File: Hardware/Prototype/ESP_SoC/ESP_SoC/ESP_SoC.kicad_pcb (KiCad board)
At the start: 4 copper layers, 34.5 x 14.7 mm, 36 parts, among them J1 USB_A, J2 Conn_01x01, J3 Conn_01x01, P1 USB_C_Plug, SW1 RESET, SW2 BOOT, U1 AP2112K-3.3, U2 ESP32-S3FN8, Y1 40MHz

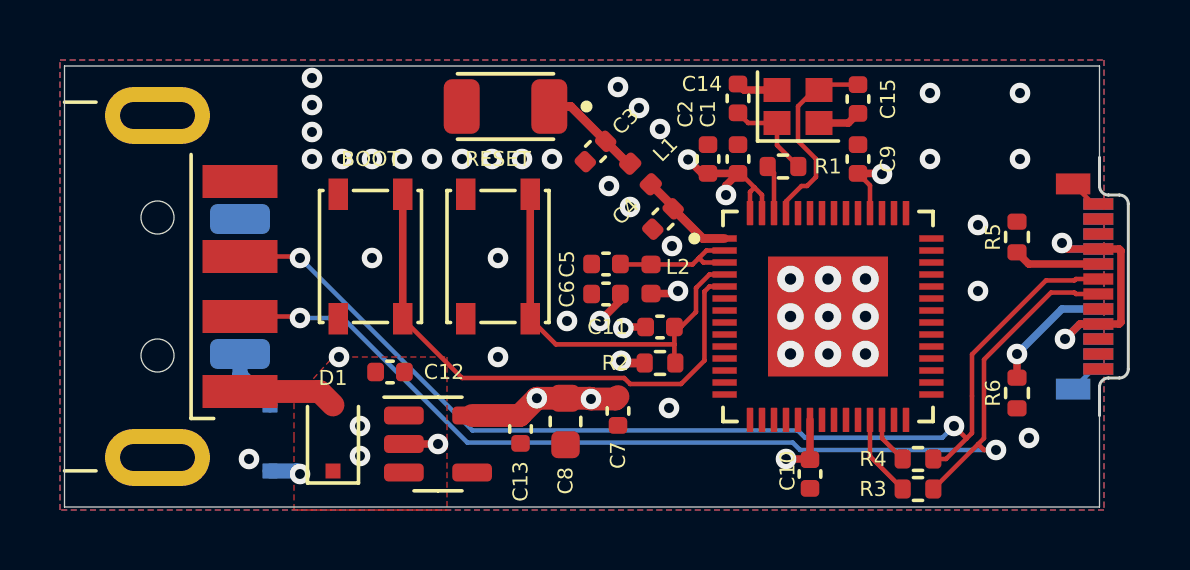
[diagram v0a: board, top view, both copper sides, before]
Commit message: Finished PCB prototypes and BOM
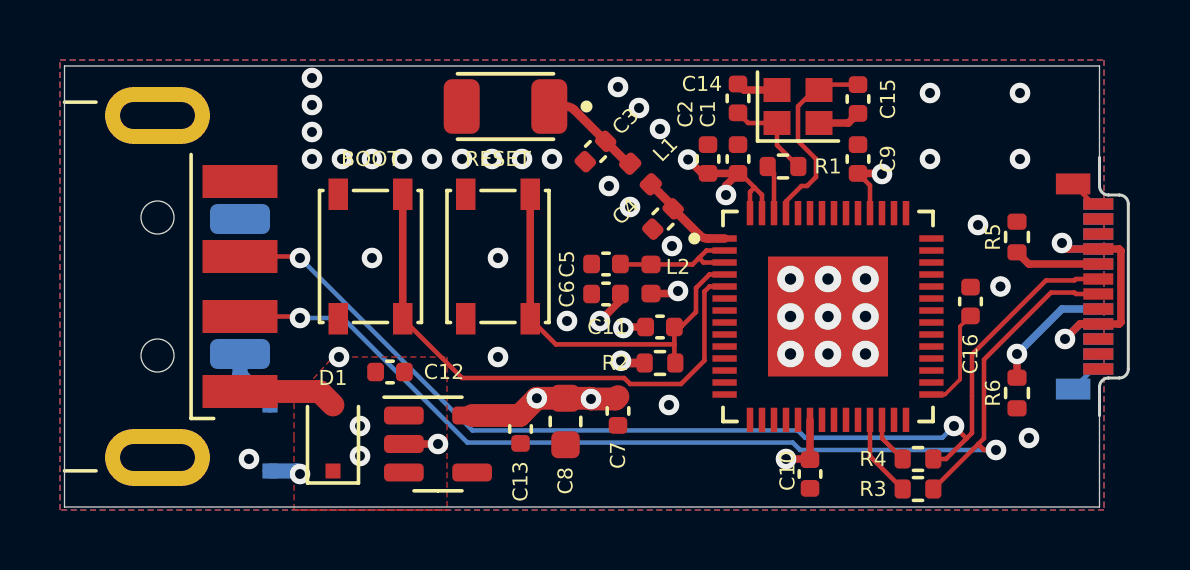
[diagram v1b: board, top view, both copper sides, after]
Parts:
- added C16: 1u, Capacitor_SMD:C_0402_1005Metric, F.Cu at (128.8, 99.2)
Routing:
- net VDD: track 0.00 -> 3.43 mm
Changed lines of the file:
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@@
     )
-  )
-  (footprint "clipboard:52b86674-39ac-4791-87c9-d1ce4ecf49a0" (layer "F.Cu")
-    (at 133.05 102.575 -90)
-    (fp_text reference "" (at 0 0 90) (layer "F.SilkS")
-      (effects (font (size 1.27 1.27) (thickness 0.15)))
-    )
-    (fp_text value "" (at 0 0 90) (layer "F.SilkS")
-      (effects (font (size 1.27 1.27) (thickness 0.15)))
-    )
-    (fp_line (start -6.875 -0.66) (end -6.875 -0.3) (layer "Edge.Cuts") (width 0.1))
-    (fp_line (start -6.575 -0.96) (end -1.075 -0.96) (layer "Edge.Cuts") (width 0.1))
-    (fp_line (start -0.475 0) (end 0.475 0) (layer "Edge.Cuts") (width 0.1))
-    (fp_line (start -0.775 -0.66) (end -0.775 -0.3) (layer "Edge.Cuts") (width 0.1))
-    (fp_line (start -7.175 0) (end -8.125 0) (layer "Edge.Cuts") (width 0.1))
-    (fp_arc (start -0.475 0) (mid -0.687132 -0.087868) (end -0.775 -0.3) (layer "Edge.Cuts") (width 0.1))
-    (fp_arc (start -6.875 -0.66) (mid -6.787132 -0.872132) (end -6.575 -0.96) (layer "Edge.Cuts") (width 0.1))
-    (fp_arc (start -6.875 -0.3) (mid -6.962868 -0.087868) (end -7.175 0) (layer "Edge.Cuts") (width 0.1))
-    (fp_arc (start -1.075 -0.96) (mid -0.862868 -0.872132) (end -0.775 -0.66) (layer "Edge.Cuts") (width 0.1))
   )
   (footprint "Inductor_SMD:L_0402_1005Metric" (layer "F.Cu")
@@
     )
   )
+  (footprint "clipboard:52b86674-39ac-4791-87c9-d1ce4ecf49a0" (layer "F.Cu")
+    (at 133.05 102.575 -90)
+    (fp_text reference "" (at 0 0 90) (layer "F.SilkS")
+      (effects (font (size 1.27 1.27) (thickness 0.15)))
+    )
+    (fp_text value "" (at 0 0 90) (layer "F.SilkS")
+      (effects (font (size 1.27 1.27) (thickness 0.15)))
+    )
+    (fp_line (start -6.875 -0.66) (end -6.875 -0.3) (layer "Edge.Cuts") (width 0.1))
+    (fp_line (start -6.575 -0.96) (end -1.075 -0.96) (layer "Edge.Cuts") (width 0.1))
+    (fp_line (start -0.475 0) (end 0.475 0) (layer "Edge.Cuts") (width 0.1))
+    (fp_line (start -0.775 -0.66) (end -0.775 -0.3) (layer "Edge.Cuts") (width 0.1))
+    (fp_line (start -7.175 0) (end -8.125 0) (layer "Edge.Cuts") (width 0.1))
+    (fp_arc (start -0.475 0) (mid -0.687132 -0.087868) (end -0.775 -0.3) (layer "Edge.Cuts") (width 0.1))
+    (fp_arc (start -6.875 -0.66) (mid -6.787132 -0.872132) (end -6.575 -0.96) (layer "Edge.Cuts") (width 0.1))
+    (fp_arc (start -6.875 -0.3) (mid -6.962868 -0.087868) (end -7.175 0) (layer "Edge.Cuts") (width 0.1))
+    (fp_arc (start -1.075 -0.96) (mid -0.862868 -0.872132) (end -0.775 -0.66) (layer "Edge.Cuts") (width 0.1))
+  )
   (footprint "Capacitor_SMD:C_0603_1608Metric" (layer "F.Cu")
     (at 115.25 103.25 -90)
@@
       (net 1 "+3V3") (pintype "passive"))
     (pad "2" smd roundrect (at 0.48 0 180) (size 0.56 0.62) (layers "F.Cu" "F.Paste" "F.Mask") (roundrect_rratio 0.25)
+      (net 2 "GND") (pintype "passive"))
+    (model "${KICAD6_3DMODEL_DIR}/Capacitor_SMD.3dshapes/C_0402_1005Metric.wrl"
+      (offset (xyz 0 0 0))
+      (scale (xyz 1 1 1))
+      (rotate (xyz 0 0 0))
+    )
+  )
+  (footprint "Capacitor_SMD:C_0402_1005Metric" (layer "F.Cu")
+    (at 128.75 99.25 90)
+    (descr "Capacitor SMD 0402 (1005 Metric), square (rectangular) end terminal, IPC_7351 nominal, (Body size source: IPC-SM-782 page 76, https://www.pcb-3d.com/wordpress/wp-content/uploads/ipc-sm-782a_amendment_1_and_2.pdf), generated with kicad-footprint-generator")
+    (tags "capacitor")
+    (property "Sheetfile" "ESP_SoC.kicad_sch")
+    (property "Sheetname" "")
+    (attr smd)
+    (fp_text reference "C16" (at -1.75 0 90) (layer "F.SilkS")
+      (effects (font (size 0.5 0.5) (thickness 0.125)))
+    )
+    (fp_text value "1u" (at 0 1.16 90) (layer "F.Fab")
+      (effects (font (size 1 1) (thickness 0.15)))
+    )
+    (fp_text user "${REFERENCE}" (at 0 0 90) (layer "F.Fab")
+      (effects (font (size 0.25 0.25) (thickness 0.04)))
+    )
+    (fp_line (start -0.107836 0.36) (end 0.107836 0.36) (layer "F.SilkS") (width 0.12))
+    (fp_line (start -0.107836 -0.36) (end 0.107836 -0.36) (layer "F.SilkS") (width 0.12))
+    (fp_line (start 0.91 0.46) (end -0.91 0.46) (layer "F.CrtYd") (width 0.05))
+    (fp_line (start -0.91 0.46) (end -0.91 -0.46) (layer "F.CrtYd") (width 0.05))
+    (fp_line (start 0.91 -0.46) (end 0.91 0.46) (layer "F.CrtYd") (width 0.05))
+    (fp_line (start -0.91 -0.46) (end 0.91 -0.46) (layer "F.CrtYd") (width 0.05))
+    (fp_line (start 0.5 -0.25) (end 0.5 0.25) (layer "F.Fab") (width 0.1))
+    (fp_line (start -0.5 -0.25) (end 0.5 -0.25) (layer "F.Fab") (width 0.1))
+    (fp_line (start -0.5 0.25) (end -0.5 -0.25) (layer "F.Fab") (width 0.1))
+    (fp_line (start 0.5 0.25) (end -0.5 0.25) (layer "F.Fab") (width 0.1))
+    (pad "1" smd roundrect (at -0.48 0 90) (size 0.56 0.62) (layers "F.Cu" "F.Paste" "F.Mask") (roundrect_rratio 0.25)
+      (net 57 "VDD") (pintype "passive"))
+    (pad "2" smd roundrect (at 0.48 0 90) (size 0.56 0.62) (layers "F.Cu" "F.Paste" "F.Mask") (roundrect_rratio 0.25)
       (net 2 "GND") (pintype "passive"))
     (model "${KICAD6_3DMODEL_DIR}/Capacitor_SMD.3dshapes/C_0402_1005Metric.wrl"
@@
   (via (at 109.8 94.5) (size 0.6858) (drill 0.3302) (layers "F.Cu" "B.Cu") (net 2))
   (via (at 114.8 94.5) (size 0.6858) (drill 0.3302) (layers "F.Cu" "B.Cu") (net 2))
-  (via (at 118.7 102.8) (size 0.6858) (drill 0.3302) (layers "F.Cu" "B.Cu") (net 2))
+  (via (at 118.7 102.7) (size 0.6858) (drill 0.3302) (layers "F.Cu" "B.Cu") (net 2))
   (via (at 124 101) (size 0.889) (drill 0.381) (layers "F.Cu" "B.Cu") (net 2))
   (via (at 118.8 97.4) (size 0.6858) (drill 0.3302) (layers "F.Cu" "B.Cu") (net 2))
@@
   (via (at 125.25 101) (size 0.889) (drill 0.381) (layers "F.Cu" "B.Cu") (net 2))
   (via (at 111.8 94.5) (size 0.6858) (drill 0.3302) (layers "F.Cu" "B.Cu") (net 2))
-  (via (at 129 98.9) (size 0.6858) (drill 0.3302) (layers "F.Cu" "B.Cu") (net 2))
+  (via (at 129.75 98.75) (size 0.6858) (drill 0.3302) (layers "F.Cu" "B.Cu") (net 2))
   (via (at 118.4 93.5) (size 0.6858) (drill 0.3302) (layers "F.Cu" "B.Cu") (net 2))
   (via (at 125.25 99.75) (size 0.889) (drill 0.381) (layers "F.Cu" "B.Cu") (net 2))
@@
   (segment (start 133.01 101.5) (end 132.84 101.5) (width 0.1542) (layer "B.Cu") (net 2))
   (segment (start 132.84 101.5) (end 132.17 102.17) (width 0.1542) (layer "B.Cu") (net 2))
-  (segment (start 119.828822 97.15) (end 118.839411 96.160589) (width 0.29337) (layer "F.Cu") (net 3))
+  (segment (start 119.711664 97.032842) (end 118.839411 96.160589) (width 0.29337) (layer "F.Cu") (net 3))
   (segment (start 118.839411 96.089411) (end 118.092947 95.342947) (width 0.29337) (layer "F.Cu") (net 3))
-  (segment (start 120.555 97.15) (end 119.828822 97.15) (width 0.29337) (layer "F.Cu") (net 3))
+  (segment (start 120.555 97.15) (end 119.994507 97.15) (width 0.29337) (layer "F.Cu") (net 3))
   (segment (start 118.839411 96.160589) (end 118.839411 96.089411) (width 0.29337) (layer "F.Cu") (net 3))
+  (arc (start 119.711664 97.032842) (mid 119.841433 97.119551) (end 119.994507 97.15) (width 0.29337) (layer "F.Cu") (net 3))
   (segment (start 117.095 98.015) (end 117.08 98) (width 0.1542) (layer "F.Cu") (net 4))
   (segment (start 119.485 98.015) (end 118.1 98.015) (width 0.1542) (layer "F.Cu") (net 4))
@@
   (segment (start 117.207456 101.8) (end 111.8 101.8) (width 0.1542) (layer "F.Cu") (net 26))
   (segment (start 117.407456 102) (end 117.207456 101.8) (width 0.1542) (layer "F.Cu") (net 26))
+  (segment (start 128.4 100.08) (end 128.4 101.85) (width 0.127) (layer "F.Cu") (net 57))
+  (segment (start 127.9 102.35) (end 127.445 102.35) (width 0.127) (layer "F.Cu") (net 57))
+  (segment (start 128.75 99.73) (end 128.4 100.08) (width 0.127) (layer "F.Cu") (net 57))
+  (segment (start 128.4 101.85) (end 127.9 102.35) (width 0.127) (layer "F.Cu") (net 57))
   (segment (start 117.335875 94.657053) (end 116.589411 93.910589) (width 0.29337) (layer "F.Cu") (net 71))
-  (segment (start 114.71 92.75) (end 115.428822 92.75) (width 0.29337) (layer "F.Cu") (net 71))
-  (segment (start 115.428822 92.75) (end 116.589411 93.910589) (width 0.29337) (layer "F.Cu") (net 71))
+  (segment (start 114.71 92.75) (end 115.263137 92.75) (width 0.29337) (layer "F.Cu") (net 71))
+  (segment (start 115.54598 92.867158) (end 116.589411 93.910589) (width 0.29337) (layer "F.Cu") (net 71))
   (segment (start 117.407053 94.657053) (end 117.335875 94.657053) (width 0.29337) (layer "F.Cu") (net 71))
+  (arc (start 115.263137 92.75) (mid 115.416211 92.780448) (end 115.54598 92.867158) (width 0.29337) (layer "F.Cu") (net 71))
   (segment (start 104.4 102.25) (end 107.05 102.25) (width 0.762) (layer "F.Cu") (net 72))
   (segment (start 107.05 102.25) (end 107.5 102.7) (width 0.762) (layer "F.Cu") (net 72))
